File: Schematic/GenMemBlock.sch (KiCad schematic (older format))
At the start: 32 parts, among them J1 MCU_HEADER, J2 ADDR_BUS, J3 DATA_BUS, J4 CART_A20, J5 CART_B10, J6 CART_B20, J7 CART_A10, J8 Conn_02x04_Odd_Even, P1 MD-CART-FINGERS-doragasu, U1 74HCT595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

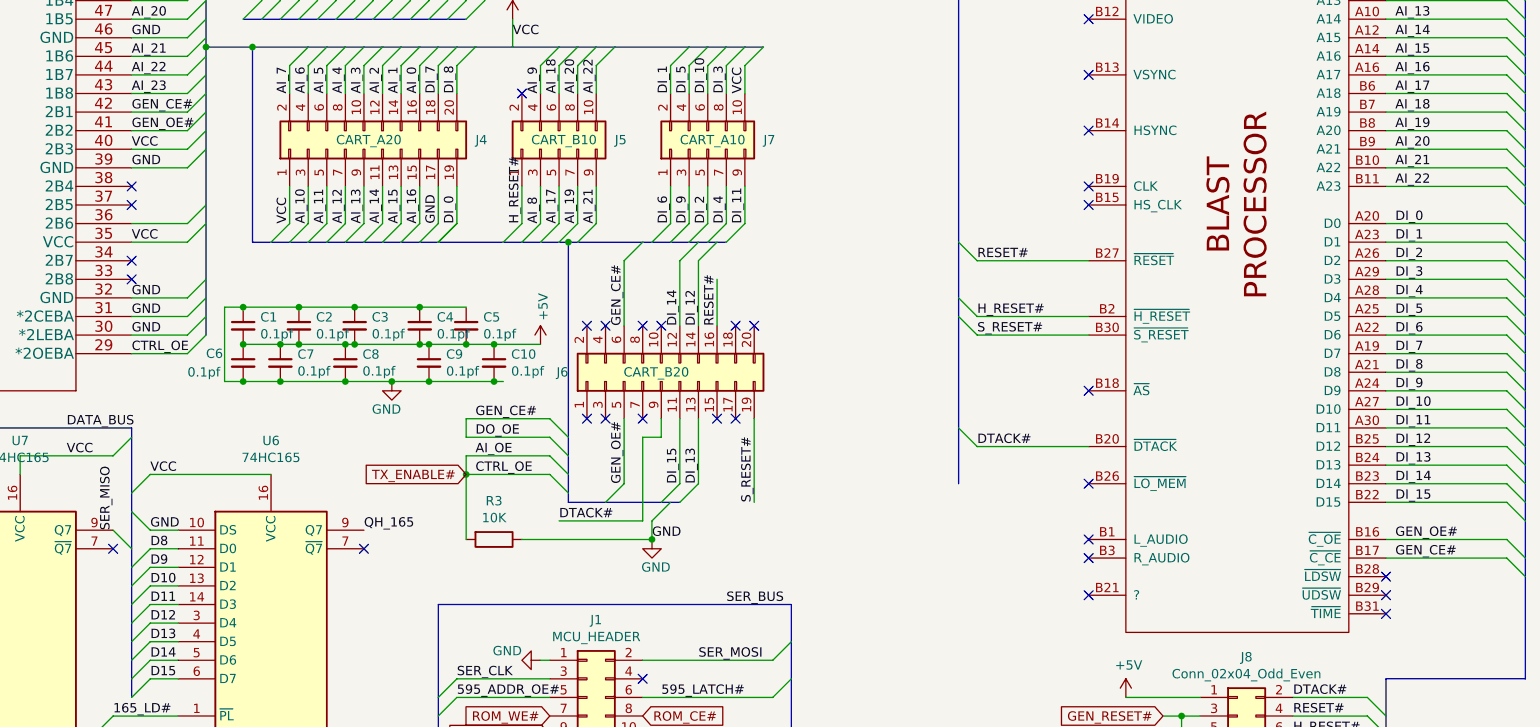
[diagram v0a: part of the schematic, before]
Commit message: propagate WE# from cart side
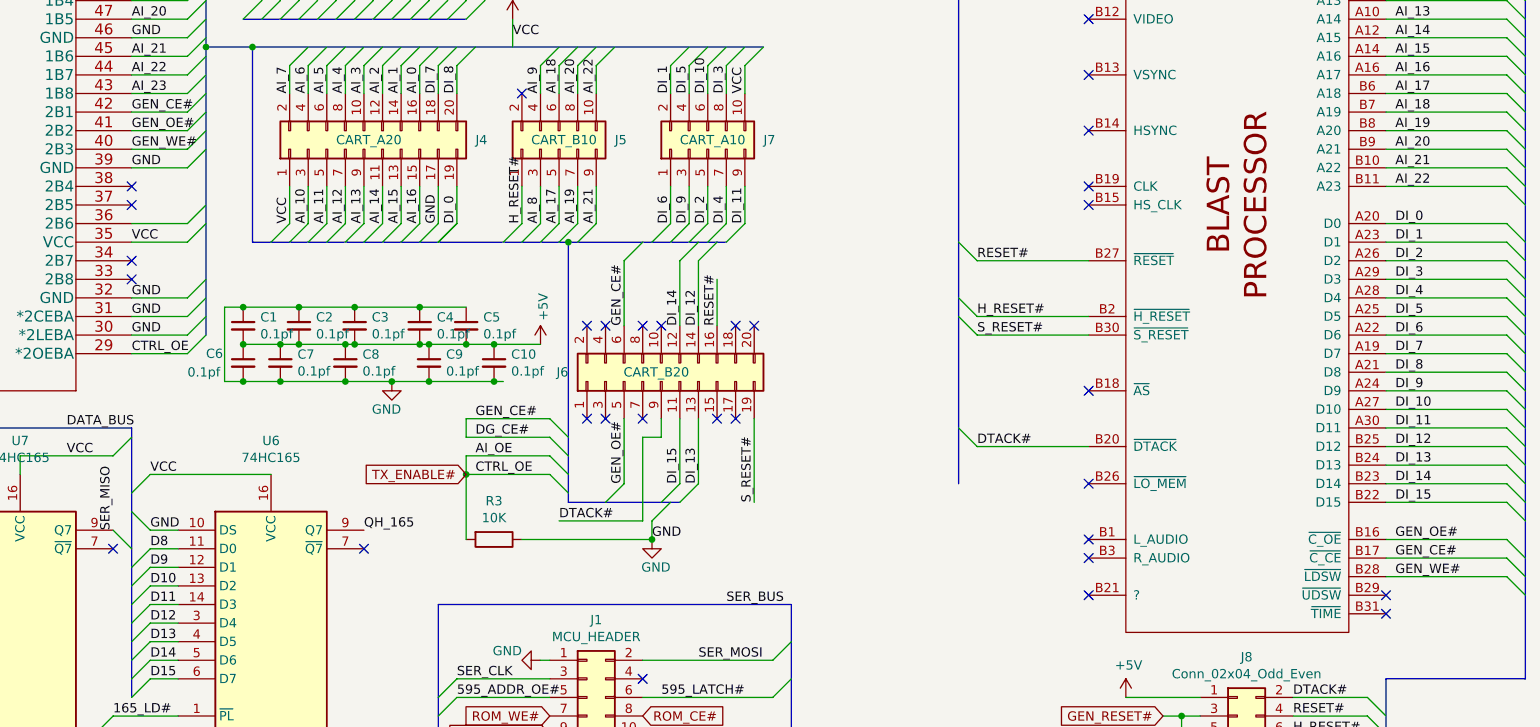
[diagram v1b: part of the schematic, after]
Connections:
- net +5V: no longer U10.40 (2B3)
- net DO_OE: no longer J6.6 (Pin_6), P1.B17 (~C_CE), U10.42 (2B1)
- net GEN_WE#: now reaches P1.B28 (~LDSW)
- net GEN_WE#: now also U10.40 (2B3)
- new net DG_CE#: J6.6 (Pin_6), P1.B17 (~C_CE), U10.42 (2B1)
- no-connect marks 44 -> 43
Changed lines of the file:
@@
 Entry Wire Line
 	2750 3800 2850 3700
-Text Label 700  1100 0    50   ~ 0
-DO_OE
 Text Label 2600 1200 0    50   ~ 0
 GND
@@
 CTRL_OE
 Text Label 9350 4250 0    50   ~ 0
-DO_OE
+DG_CE#
 Text GLabel 9300 4450 0    50   Input ~ 0
 TX_ENABLE#
@@
 Text Label 700  3800 0    50   ~ 0
 DO_OE
-Text Label 700  1300 0    50   ~ 0
-GND
 Text Label 2600 1300 0    50   ~ 0
 VCC
@@
 Text Label 7600 4750 0    50   ~ 0
 GND
-Text Label 7500 2700 0    50   ~ 0
-VCC
 $Comp
 L power:GND #PWR0114
@@
 Text Label 14300 4800 0    50   ~ 0
 GEN_OE#
-NoConn ~ 14250 5000
 NoConn ~ 14250 5100
 NoConn ~ 14250 5200
@@
 Wire Wire Line
 	9300 4250 9750 4250
+Text Label 9350 4150 0    50   ~ 0
+GEN_CE#
+Entry Wire Line
+	14900 5000 15000 5100
+Text Label 14300 5000 0    50   ~ 0
+GEN_WE#
+Wire Wire Line
+	14250 5000 14900 5000
+Text Label 700  1100 0    50   ~ 0
+DO_OE
+Text Label 700  1300 0    50   ~ 0
+GND
+Text Label 7500 2700 0    50   ~ 0
+GEN_WE#
 Wire Bus Line
 	5950 6450 7300 6450
@@
 	11050 5150 11050 6150
 Wire Bus Line
+	14250 5550 14250 6050
+Wire Bus Line
+	11950 100  11950 4500
+Wire Bus Line
 	9850 4600 10450 4600
 Wire Bus Line
@@
 	2550 4550 2550 5650
 Wire Bus Line
-	14250 5550 14250 6050
-Wire Bus Line
-	11950 100  11950 4500
+	600  950  600  1500
 Wire Bus Line
 	600  3600 600  4150
 Wire Bus Line
-	600  950  600  1500
-Wire Bus Line
 	4150 6650 4150 7650
 Wire Bus Line
@@
 Wire Bus Line
 	15000 100  15000 5550
-Text Label 9350 4150 0    50   ~ 0
-GEN_CE#
 $EndSCHEMATC
